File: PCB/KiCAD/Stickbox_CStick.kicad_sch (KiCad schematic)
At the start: 18 parts, among them U3 MCP3002, U4 DRV5055A2xDBZxQ1, U5 Stickbox_Assembly_CStick, U9 DRV5055A2xDBZxQ1

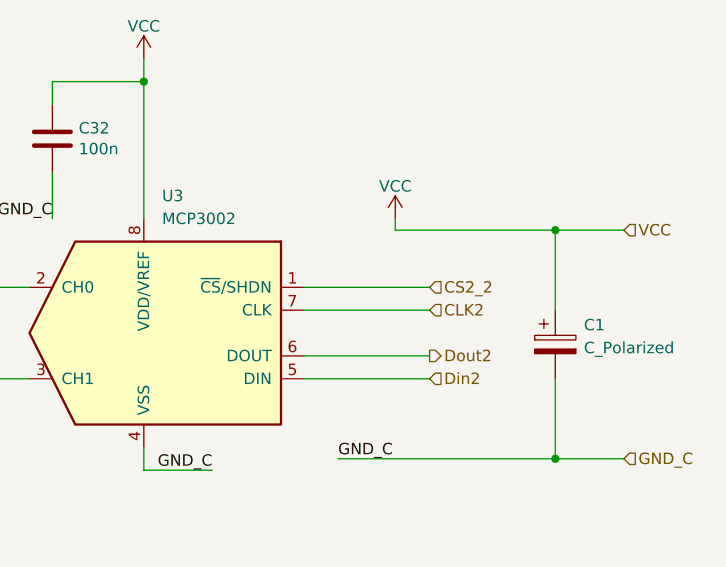
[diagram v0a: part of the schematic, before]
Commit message: Assembly and fab upload
Upload schematic pdf and bom csv and ibom html docs
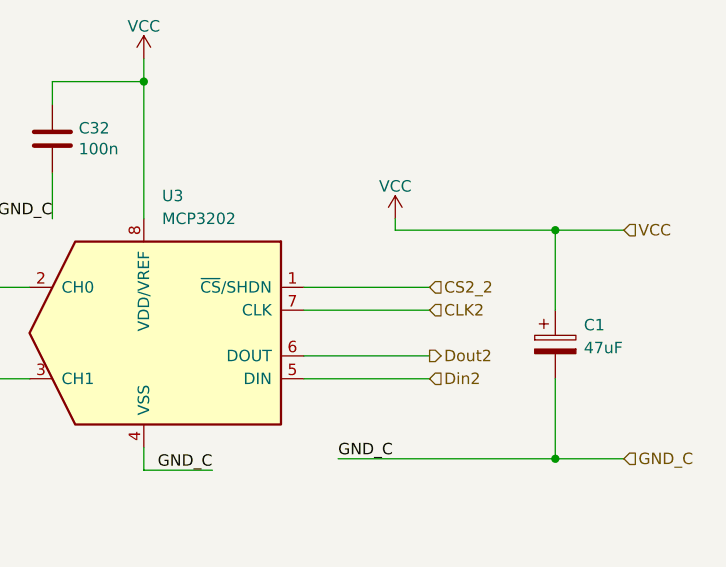
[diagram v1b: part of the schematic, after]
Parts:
- C1: value C_Polarized -> 47uF; MPN (none) -> GRM32ER71A476ME15L; Manufacturer (none) -> Murata Electronics; Package (none) -> 1210; VARIANT (none) -> NoVar
- C10, C9: MPN (none) -> CL10B104KB8NNWC; Manufacturer (none) -> Samsung Electro-Mechanics; Package (none) -> 0603; VARIANT (none) -> NoVar
- C32: MPN (none) -> CL05B104KA5NNNC; Manufacturer (none) -> Samsung Electro-Mechanics; Package (none) -> 0402; VARIANT (none) -> NoVar
- C4, C5: MPN (none) -> CL10B473KB8NNNC; Manufacturer (none) -> Samsung Electro-Mechanics; Package (none) -> 0603; VARIANT (none) -> NoVar
- H10, H11, H12, H13, H14, H15: DNP (none) -> DNP; Package (none) -> Mechanical; VARIANT (none) -> NoVar
- R3, R4: MPN (none) -> RC0603FR-132KL; Manufacturer (none) -> YAGEO; Package (none) -> 0603; VARIANT (none) -> NoVar
- U3: value MCP3002 -> MCP3202; MPN (none) -> MCP3202-CI/SN; Manufacturer (none) -> Microchip Technology; Package (none) -> 8-SOIC; VARIANT (none) -> NoVar
- U4, U9: LCSC (none) -> C266128; MPN (none) -> DRV5055A3QDBZR; Manufacturer (none) -> Texas Instruments; Package (none) -> SOT-23; VARIANT (none) -> NoVar
- U5: MPN (none) -> T3+Magnet_Assy; Manufacturer (none) -> Internal; Package (none) -> Through-hole; VARIANT (none) -> NoVar
